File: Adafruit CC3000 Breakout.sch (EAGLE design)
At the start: 33 parts, among them IC1 ATmega1284P, U1 CC3000MOD, X1 2500AT44M0400E

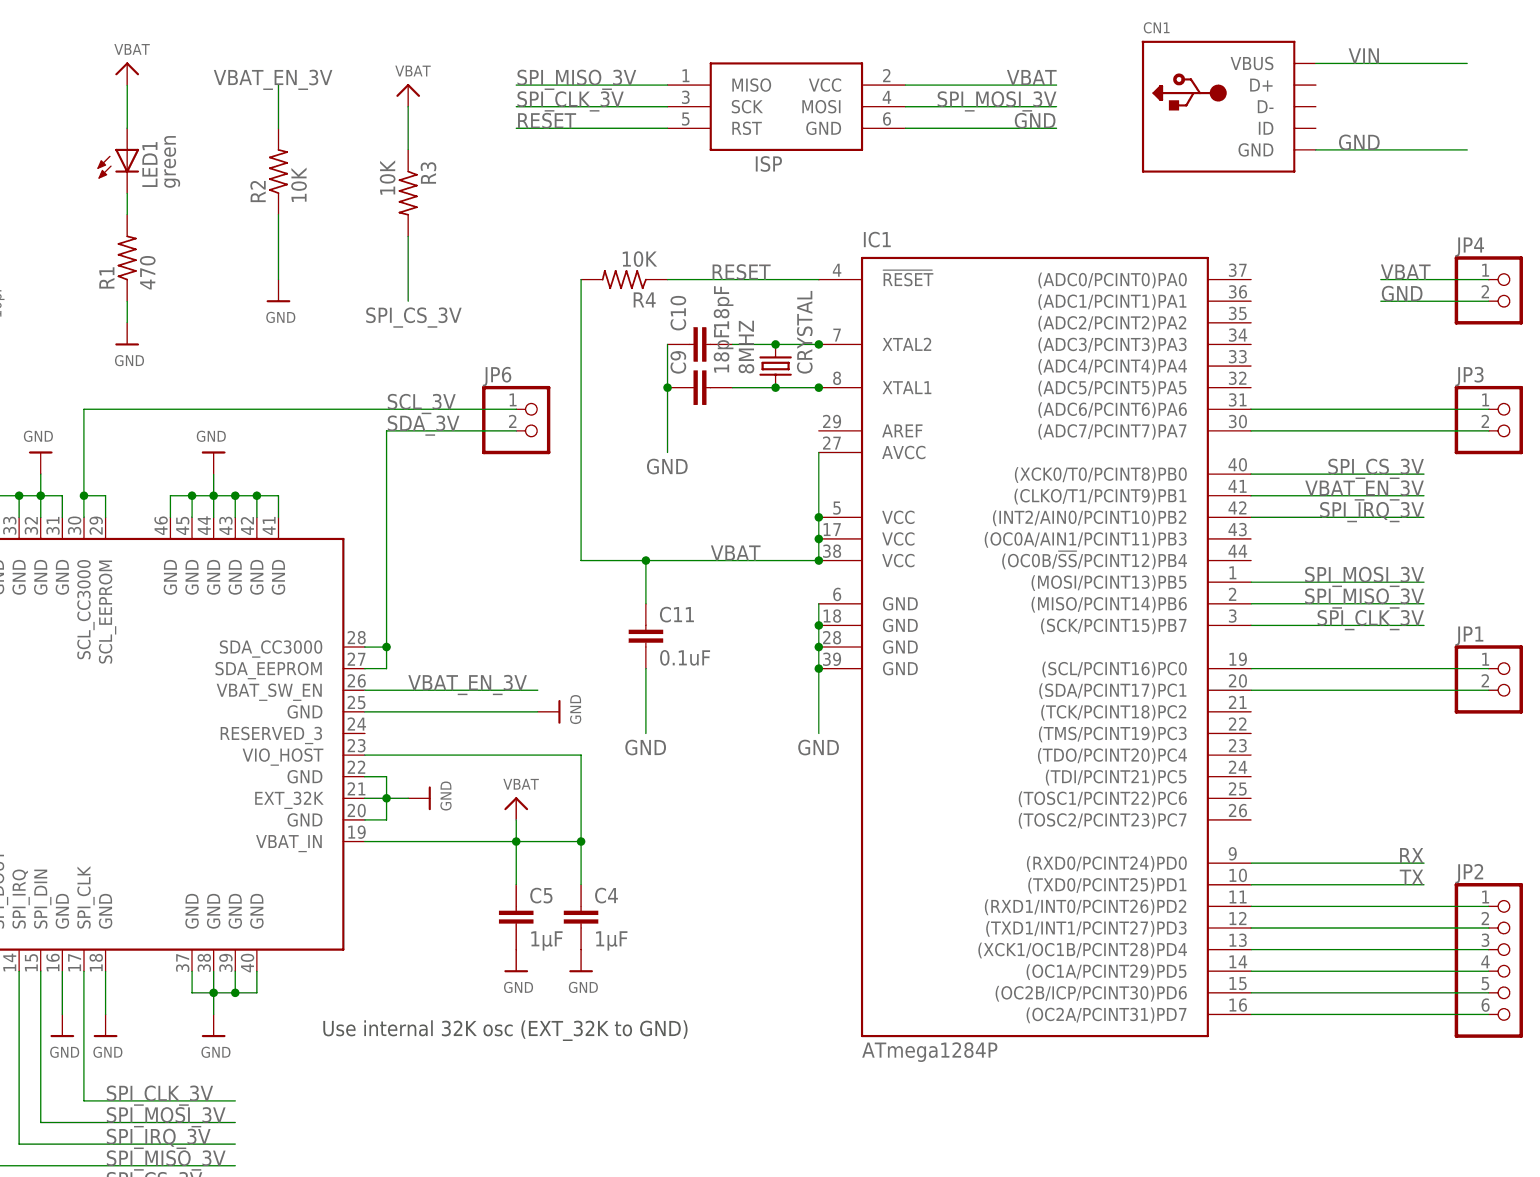
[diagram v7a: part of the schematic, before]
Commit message: Silk screen (and name some traces).
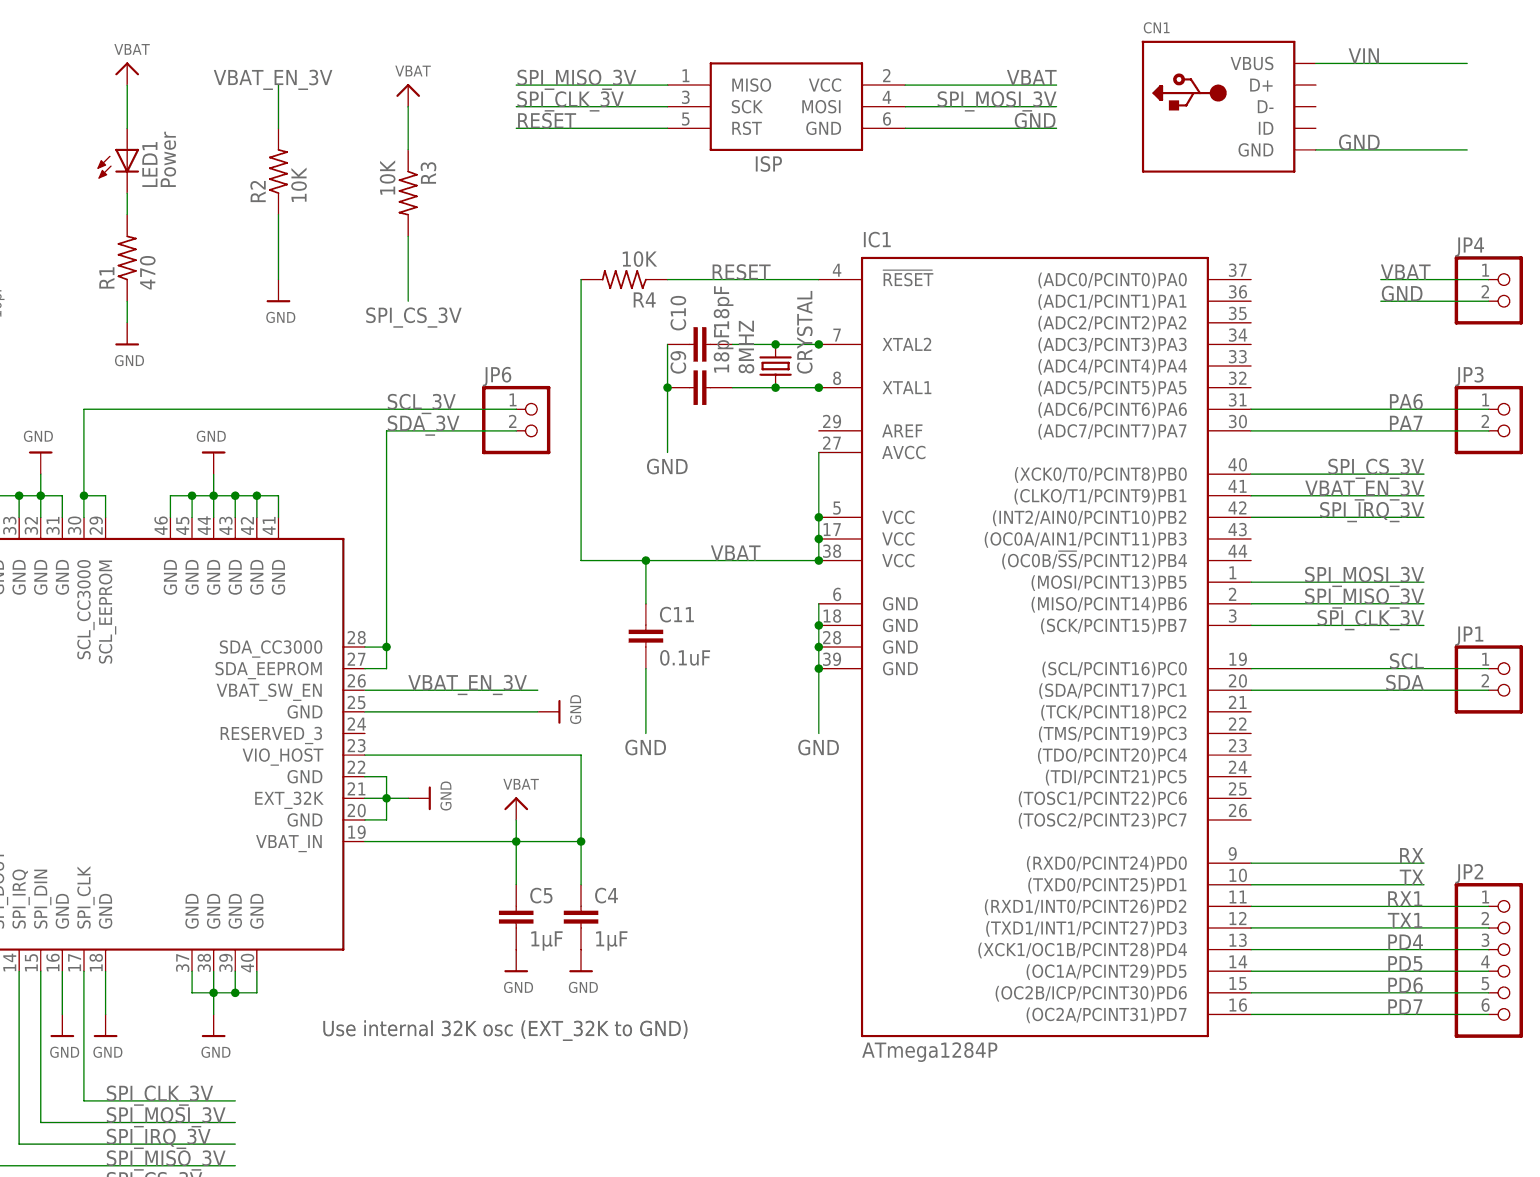
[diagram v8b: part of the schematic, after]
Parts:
- LED1: value green -> Power
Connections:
- net N$11 renamed RX1
- net N$12 renamed TX1
- net N$13 renamed PD4
- net N$14 renamed PD5
- net N$15 renamed PD6
- net N$16 renamed PD7
- net N$17 renamed PA6
- net N$18 renamed PA7
- net N$5 renamed SCL
- net N$9 renamed SDA
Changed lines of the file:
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@@
 <part name="U$22" library="microbuilder" deviceset="VBAT" device=""/>
 <part name="U$35" library="microbuilder" deviceset="U.FL" device=""/>
-<part name="LED1" library="led" deviceset="LED" device="SMT1206" value="green"/>
+<part name="LED1" library="led" deviceset="LED" device="SMT1206" value="Power"/>
 <part name="R1" library="rcl" deviceset="R-US_" device="R1206" value="470"/>
 <part name="U$37" library="microbuilder" deviceset="GND" device=""/>
@@
 </segment>
 </net>
-<net name="N$5" class="0">
+<net name="SCL" class="0">
 <segment>
 <pinref part="IC1" gate="G$1" pin="(SCL/PCINT16)PC0"/>
 <pinref part="JP1" gate="G$1" pin="1"/>
 <wire x1="251.46" y1="93.98" x2="223.52" y2="93.98" width="0.1524" layer="91"/>
-</segment>
-</net>
-<net name="N$9" class="0">
+<label x="243.84" y="93.98" size="1.778" layer="95" rot="MR0"/>
+</segment>
+</net>
+<net name="SDA" class="0">
 <segment>
 <pinref part="IC1" gate="G$1" pin="(SDA/PCINT17)PC1"/>
 <pinref part="JP1" gate="G$1" pin="2"/>
 <wire x1="251.46" y1="91.44" x2="223.52" y2="91.44" width="0.1524" layer="91"/>
-</segment>
-</net>
-<net name="N$11" class="0">
+<label x="243.84" y="91.44" size="1.778" layer="95" rot="MR0"/>
+</segment>
+</net>
+<net name="RX1" class="0">
 <segment>
 <pinref part="IC1" gate="G$1" pin="(RXD1/INT0/PCINT26)PD2"/>
 <pinref part="JP2" gate="A" pin="1"/>
 <wire x1="251.46" y1="66.04" x2="223.52" y2="66.04" width="0.1524" layer="91"/>
-</segment>
-</net>
-<net name="N$12" class="0">
+<label x="243.84" y="66.04" size="1.778" layer="95" rot="MR0"/>
+</segment>
+</net>
+<net name="TX1" class="0">
 <segment>
 <pinref part="IC1" gate="G$1" pin="(TXD1/INT1/PCINT27)PD3"/>
 <pinref part="JP2" gate="A" pin="2"/>
 <wire x1="251.46" y1="63.5" x2="223.52" y2="63.5" width="0.1524" layer="91"/>
-</segment>
-</net>
-<net name="N$13" class="0">
+<label x="243.84" y="63.5" size="1.778" layer="95" rot="MR0"/>
+</segment>
+</net>
+<net name="PD4" class="0">
 <segment>
 <pinref part="IC1" gate="G$1" pin="(XCK1/OC1B/PCINT28)PD4"/>
 <pinref part="JP2" gate="A" pin="3"/>
 <wire x1="251.46" y1="60.96" x2="223.52" y2="60.96" width="0.1524" layer="91"/>
-</segment>
-</net>
-<net name="N$14" class="0">
+<label x="243.84" y="60.96" size="1.778" layer="95" rot="MR0"/>
+</segment>
+</net>
+<net name="PD5" class="0">
 <segment>
 <pinref part="IC1" gate="G$1" pin="(OC1A/PCINT29)PD5"/>
 <pinref part="JP2" gate="A" pin="4"/>
 <wire x1="251.46" y1="58.42" x2="223.52" y2="58.42" width="0.1524" layer="91"/>
-</segment>
-</net>
-<net name="N$15" class="0">
+<label x="243.84" y="58.42" size="1.778" layer="95" rot="MR0"/>
+</segment>
+</net>
+<net name="PD6" class="0">
 <segment>
 <pinref part="IC1" gate="G$1" pin="(OC2B/ICP/PCINT30)PD6"/>
 <pinref part="JP2" gate="A" pin="5"/>
 <wire x1="251.46" y1="55.88" x2="223.52" y2="55.88" width="0.1524" layer="91"/>
-</segment>
-</net>
-<net name="N$16" class="0">
+<label x="243.84" y="55.88" size="1.778" layer="95" rot="MR0"/>
+</segment>
+</net>
+<net name="PD7" class="0">
 <segment>
 <pinref part="IC1" gate="G$1" pin="(OC2A/PCINT31)PD7"/>
 <pinref part="JP2" gate="A" pin="6"/>
 <wire x1="251.46" y1="53.34" x2="223.52" y2="53.34" width="0.1524" layer="91"/>
-</segment>
-</net>
-<net name="N$17" class="0">
+<label x="243.84" y="53.34" size="1.778" layer="95" rot="MR0"/>
+</segment>
+</net>
+<net name="PA6" class="0">
 <segment>
 <pinref part="IC1" gate="G$1" pin="(ADC6/PCINT6)PA6"/>
 <pinref part="JP3" gate="G$1" pin="1"/>
 <wire x1="251.46" y1="124.46" x2="223.52" y2="124.46" width="0.1524" layer="91"/>
-</segment>
-</net>
-<net name="N$18" class="0">
+<label x="243.84" y="124.46" size="1.778" layer="95" rot="MR0"/>
+</segment>
+</net>
+<net name="PA7" class="0">
 <segment>
 <pinref part="IC1" gate="G$1" pin="(ADC7/PCINT7)PA7"/>
 <pinref part="JP3" gate="G$1" pin="2"/>
 <wire x1="251.46" y1="121.92" x2="223.52" y2="121.92" width="0.1524" layer="91"/>
-</segment>
-</net>
+<label x="243.84" y="121.92" size="1.778" layer="95" rot="MR0"/>
+</segment>
+</net>
